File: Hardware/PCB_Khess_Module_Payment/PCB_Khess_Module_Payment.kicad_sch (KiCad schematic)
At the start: 54 parts, among them IC1 SI4435DDY-T1-GE3, IC2 MCP73844-840I_MS, J1 Conn_02x20_Odd_Even, J2 Conn_01x02, J3 Conn_01x08, J4 Conn_01x04, J5 USB_C_Receptacle_USB2.0, J6 Conn_01x08, U1 FSV330AF, U2 FSV330AF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

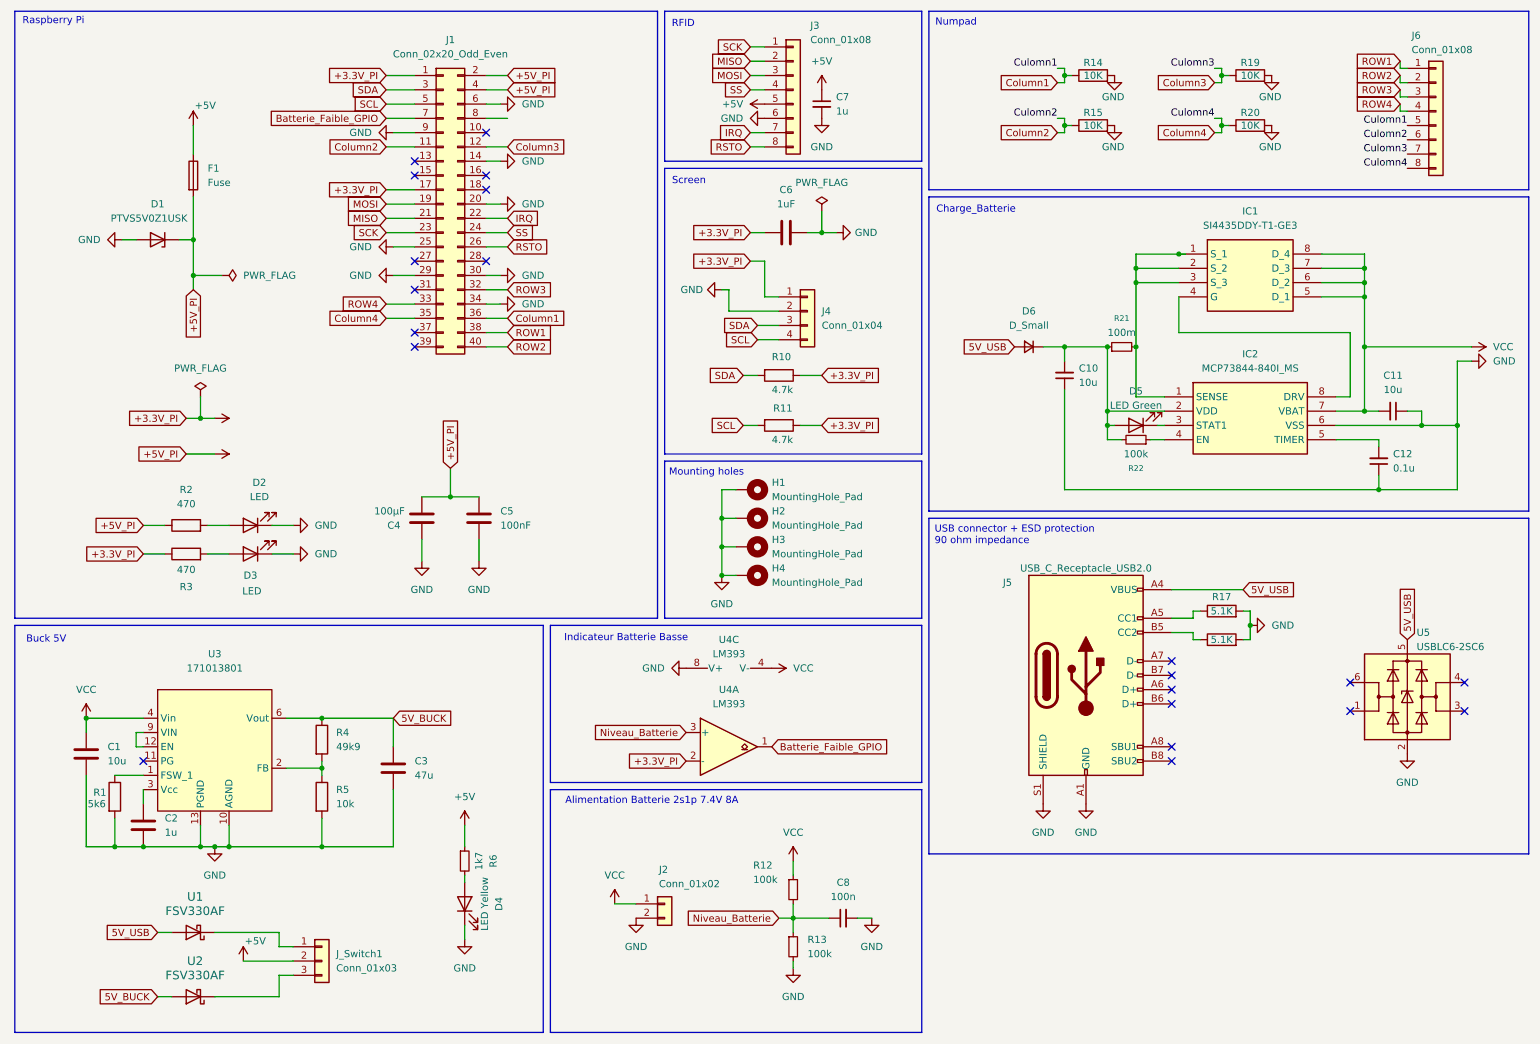
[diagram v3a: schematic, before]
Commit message: fix: usb c to 12v dc barel jack connector
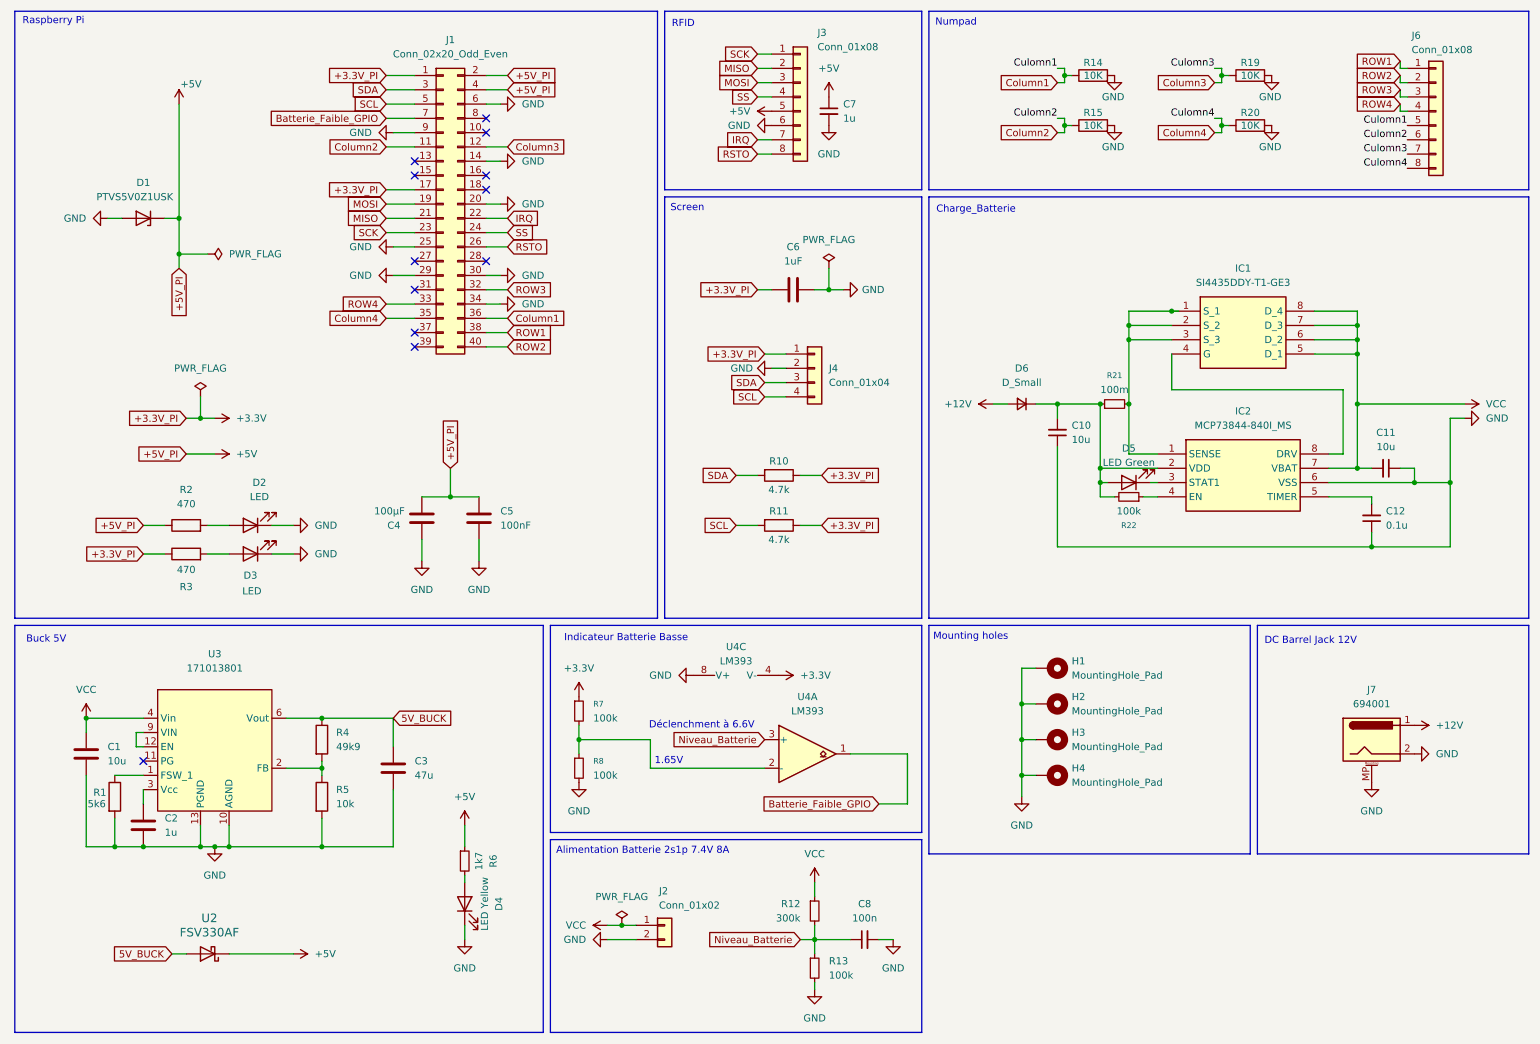
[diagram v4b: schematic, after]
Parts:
- removed F1: Fuse, Fuse:FuseHolder_Blade_ATO_Littelfuse_FLR_178.6165, symbol Device:Fuse
- removed J5: USB_C_Receptacle_USB2.0, Connector_USB:USB_C_Receptacle_HRO_TYPE-C-31-M-12, symbol Connector:USB_C_Receptacle_USB2.0
- removed J_Switch1: Conn_01x03, Connector_JST:JST_XA_S03B-XASK-1_1x03_P2.50mm_Horizontal, symbol Connector_Generic:Conn_01x03
- removed R17, R18: 5.1K, Resistor_SMD:R_0603_1608Metric_Pad0.98x0.95mm_HandSolder, symbol Device:R
- removed U1: FSV330AF, Diode_SMD:D_SOD-123, symbol Device:D_Schottky
- removed U5: USBLC6-2SC6, Package_TO_SOT_SMD:SOT-23-6, symbol Power_Protection:USBLC6-2SC6
- added J7: 694001, Connector_BarrelJack:BarrelJack_Wuerth_6941xx301002, symbol Connector:Barrel_Jack_MountingPin
- added R7, R8: 100k, symbol Device:R_Small
- IC1: footprint SOIC127P600X175-8N -> SI4435DDY-T1-GE3:SOIC127P600X175-8N
- IC2: footprint SOP65P490X110-8N -> MCP73844-840I_MS:SOP65P490X110-8N
- R12: value 100k -> 300k
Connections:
- net +3.3V: now also U4.4 (V-), R7.1; no longer U4.2 (-)
- net +5V: now also U2.1 (K)
- net GND: now also J7.2, J7.MP (MountPin), R8.2
- net VCC: no longer U4.4 (V-)
- net 5V_USB renamed +12V
- net +12V: now also J7.1
- new net: R7.2, R8.1, U4.2 (-)
- no-connect marks 21 -> 12
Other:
- note added: "1.65V"
- note added: "DC Barrel Jack 12V"
- note added: "Déclenchment à 6.6V"
- note removed: "USB connector + ESD protection 90 ohm impedance"
- moved on the sheet: C10, C11, C12, C6, C7, C8, D1, D5, D6, H1, H2, H3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
